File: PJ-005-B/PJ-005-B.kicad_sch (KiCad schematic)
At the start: 0 parts

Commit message: -- Transmitter with pre-amp LM7171 and power amp LT1210 -- Receiver with charge amp-->inverting amp-->4th order filter-->Inverting amp-->buffer -- Power with LDO 12V to 9V, 9V to 6V, 6V to 5V, 5V to 2.5V and -5V to -2.5V
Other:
- company: (none) -> Xalten Systems Pvt. Ltd.
- title: (none) -> Echosounder Transceiver
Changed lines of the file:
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@@
 	(generator_version "9.0")
 	(paper "A4")
+	(title_block
+		(title "Echosounder Transceiver")
+		(date "06-04-2026")
+		(rev "0.1")
+		(company "Xalten Systems Pvt. Ltd.")
+		(comment 1 "Designed by: Varun G")
+	)
 	(sheet
 		(at 158.75 34.29)

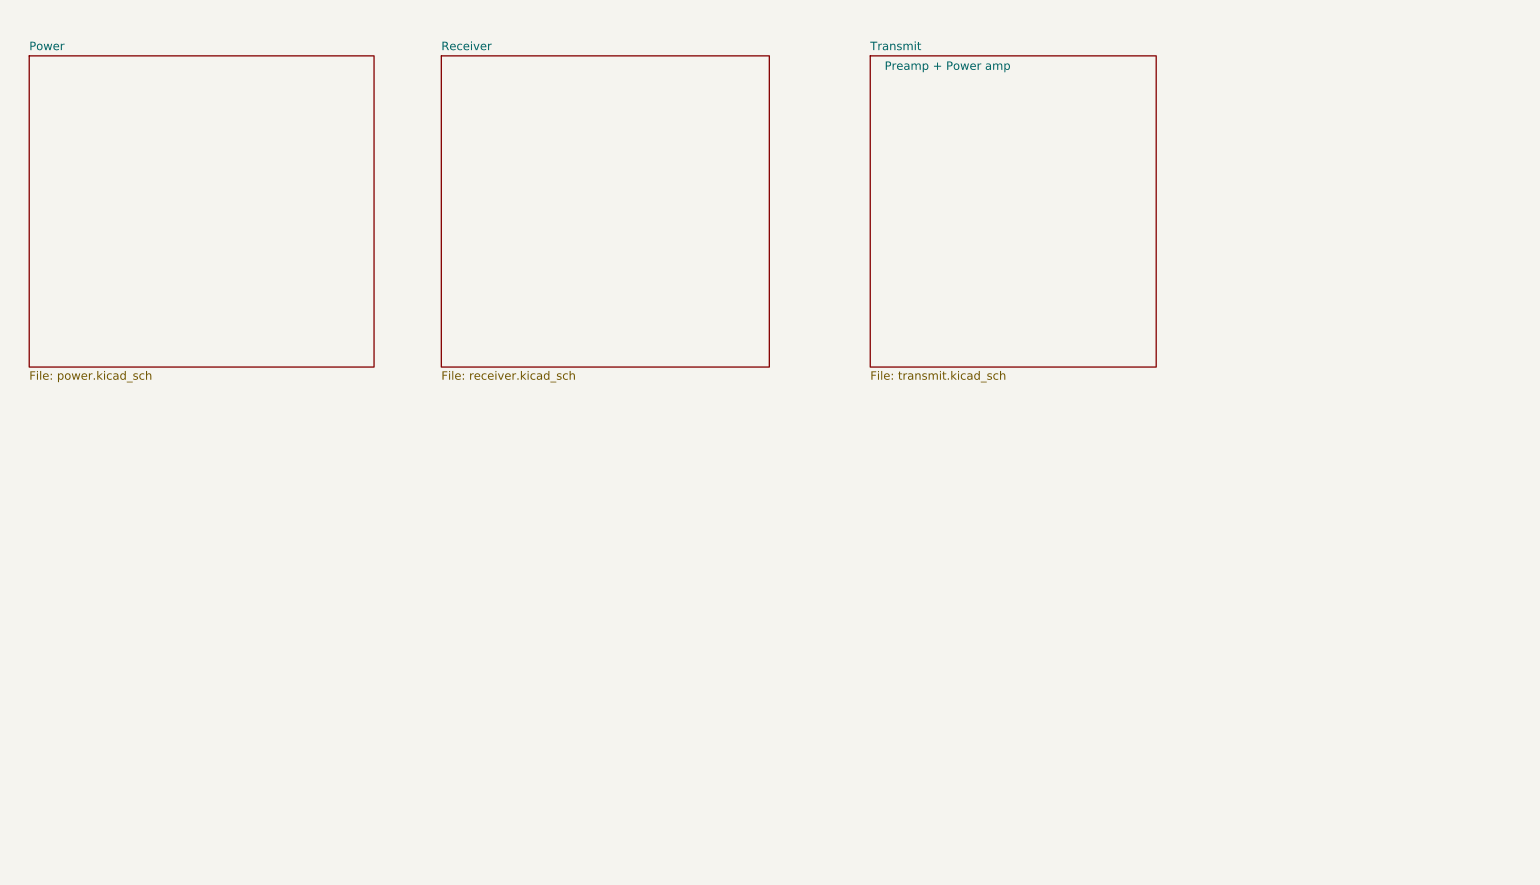
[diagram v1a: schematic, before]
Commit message: -- Receive stage with charge amp-->inverting amp-->BPF-->inverting amp-->buffer-->PGA-->buffer -- Transmit stage with push pull mosfet -- TTL to RS485 converter -- LDOs 12V to 9V, 9V to 6V, 6V to 5V, 5V to 2.5V and -5V to -2.5V
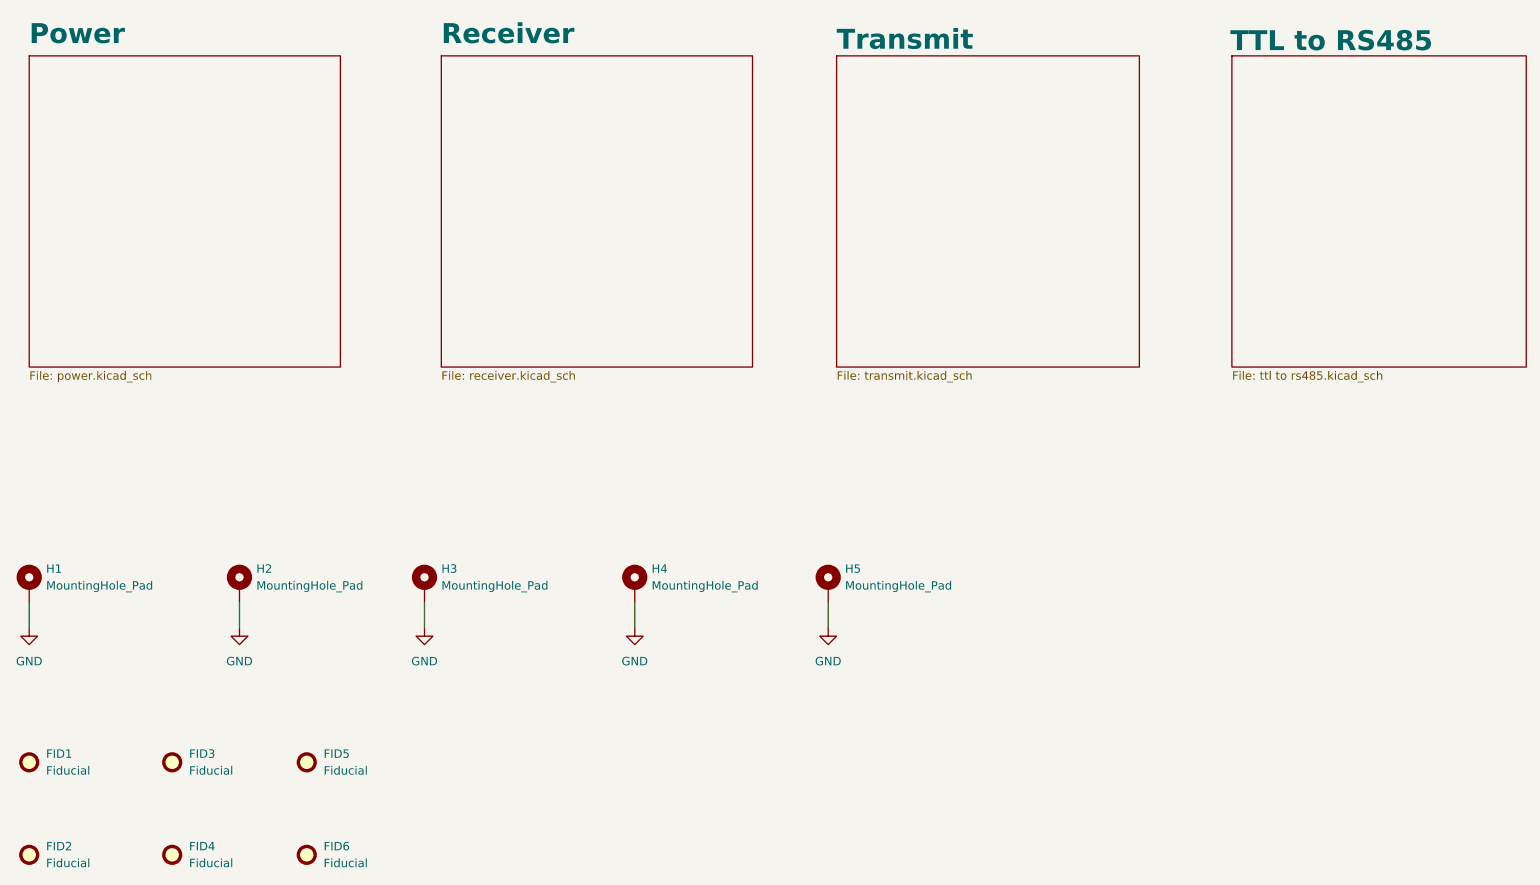
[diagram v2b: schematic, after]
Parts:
- added FID1, FID2, FID3, FID4, FID5, FID6: Fiducial, Fiducial:Fiducial_0.5mm_Mask1mm, symbol Mechanical:Fiducial
- added H1, H2, H3, H4, H5: MountingHole_Pad, MountingHole:MountingHole_3.2mm_M3_DIN965_Pad, symbol Mechanical:MountingHole_Pad
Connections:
- new net GND: H1.1, H2.1, H3.1, H4.1, H5.1
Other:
- added sheet TTL to RS485 (ttl to rs485.kicad_sch)
